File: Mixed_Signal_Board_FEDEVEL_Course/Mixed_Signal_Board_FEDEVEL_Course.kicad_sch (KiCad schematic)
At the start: 0 parts

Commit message: Add Bi filter for Power Sheet
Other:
- added sheet Mixed_Signal_Board_Power (Mixed_Signal_Board_Power.kicad_sch)
- note added: "Hardware Design for Analog Signal Acquisition and Generation Using ADC and DAC"
- note added: "Mixed Signal Board"
- title: (none) -> ${Project_Name}
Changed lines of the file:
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@@
 	(generator_version "10.0")
 	(paper "A4")
+	(title_block
+		(title "${Project_Name}")
+		(date "2026-03-29")
+		(rev "A")
+	)
+	(text "Hardware Design for Analog Signal Acquisition and Generation Using ADC and DAC\n"
+		(exclude_from_sim no)
+		(at 143.51 41.91 0)
+		(effects
+			(font
+				(size 1.27 1.27)
+				(thickness 0.254)
+				(bold yes)
+			)
+		)
+	)
+	(text "Mixed Signal Board"
+		(exclude_from_sim no)
+		(at 144.78 35.56 0)
+		(effects
+			(font
+				(size 4 4)
+				(thickness 0.8)
+				(bold yes)
+				(italic yes)
+				(color 132 0 0 1)
+			)
+		)
+	)
+	(sheet
+		(at 63.5 64.77)
+		(size 41.91 48.26)
+		(exclude_from_sim no)
+		(in_bom yes)
+		(on_board yes)
+		(dnp no)
+		(fields_autoplaced yes)
+		(stroke
+			(width 0.1524)
+			(type solid)
+		)
+		(fill
+			(color 255 255 194 1)
+		)
+		(property "Sheetname" "Mixed_Signal_Board_Power"
+			(at 63.5 64.0584 0)
+			(show_name no)
+			(do_not_autoplace no)
+			(effects
+				(font
+					(size 1.27 1.27)
+				)
+				(justify left bottom)
+			)
+		)
+		(property "Sheetfile" "Mixed_Signal_Board_Power.kicad_sch"
+			(at 63.5 113.6146 0)
+			(show_name no)
+			(do_not_autoplace no)
+			(effects
+				(font
+					(size 1.27 1.27)
+				)
+				(justify left top)
+			)
+		)
+		(instances
+			(project "Mixed_Signal_Board_FEDEVEL_Course"
+				(path "/275c6be1-327e-4739-aa63-a3cb51a55660"
+					(page "2")
+				)
+			)
+		)
+	)
 	(sheet_instances
 		(path "/"

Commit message: Create controller sheet
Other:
- added sheet Mixed_Signal_Board_MCU (Mixed_Signal_Board_MCU.kicad_sch)
- note added: "[1] Power"
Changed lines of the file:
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@@
+		)
+	)
+	(text "[1] Power"
+		(exclude_from_sim no)
+		(at 85.09 88.9 0)
+		(effects
+			(font
+				(size 4 4)
+				(thickness 0.8)
+				(bold yes)
+				(italic yes)
+				(color 0 0 255 1)
+			)
 		)
 	)
@@
 				)
 			)
+		)
+	)
+	(sheet
+		(at 152.4 64.77)
+		(size 43.18 48.26)
+		(exclude_from_sim no)
+		(in_bom yes)
+		(on_board yes)
+		(dnp no)
+		(fields_autoplaced yes)
+		(stroke
+			(width 0.1524)
+			(type solid)
+		)
+		(fill
+			(color 255 255 194 1)
+		)
+		(property "Sheetname" "Mixed_Signal_Board_MCU"
+			(at 152.4 64.0584 0)
+			(show_name no)
+			(do_not_autoplace no)
+			(effects
+				(font
+					(size 1.27 1.27)
+				)
+				(justify left bottom)
+			)
+		)
+		(property "Sheetfile" "Mixed_Signal_Board_MCU.kicad_sch"
+			(at 152.4 113.6146 0)
+			(show_name no)
+			(do_not_autoplace no)
+			(effects
+				(font
+					(size 1.27 1.27)
+				)
+				(justify left top)
+			)
+		)
+		(instances
+			(project "Mixed_Signal_Board_FEDEVEL_Course"
+				(path "/275c6be1-327e-4739-aa63-a3cb51a55660"
+					(page "3")
+				)
+			)

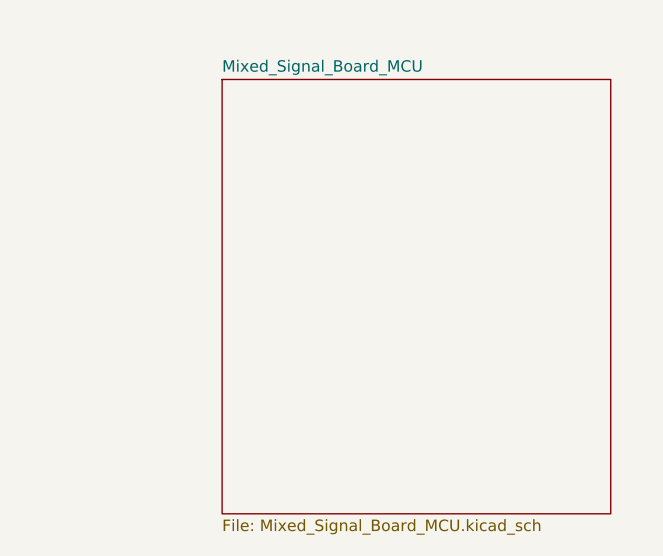
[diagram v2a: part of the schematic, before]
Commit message: Add oscillator circuit for MCU sheet
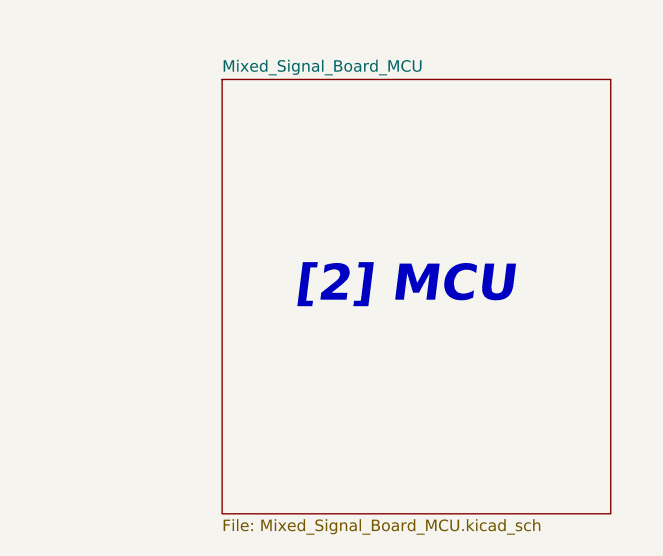
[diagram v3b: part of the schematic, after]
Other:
- note added: "[2] MCU"
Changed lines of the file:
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@@
+		)
+	)
+	(text "[2] MCU\n"
+		(exclude_from_sim no)
+		(at 172.72 87.63 0)
+		(effects
+			(font
+				(size 4 4)
+				(thickness 0.8)
+				(bold yes)
+				(italic yes)
+				(color 0 0 255 1)
+			)
 		)
 	)

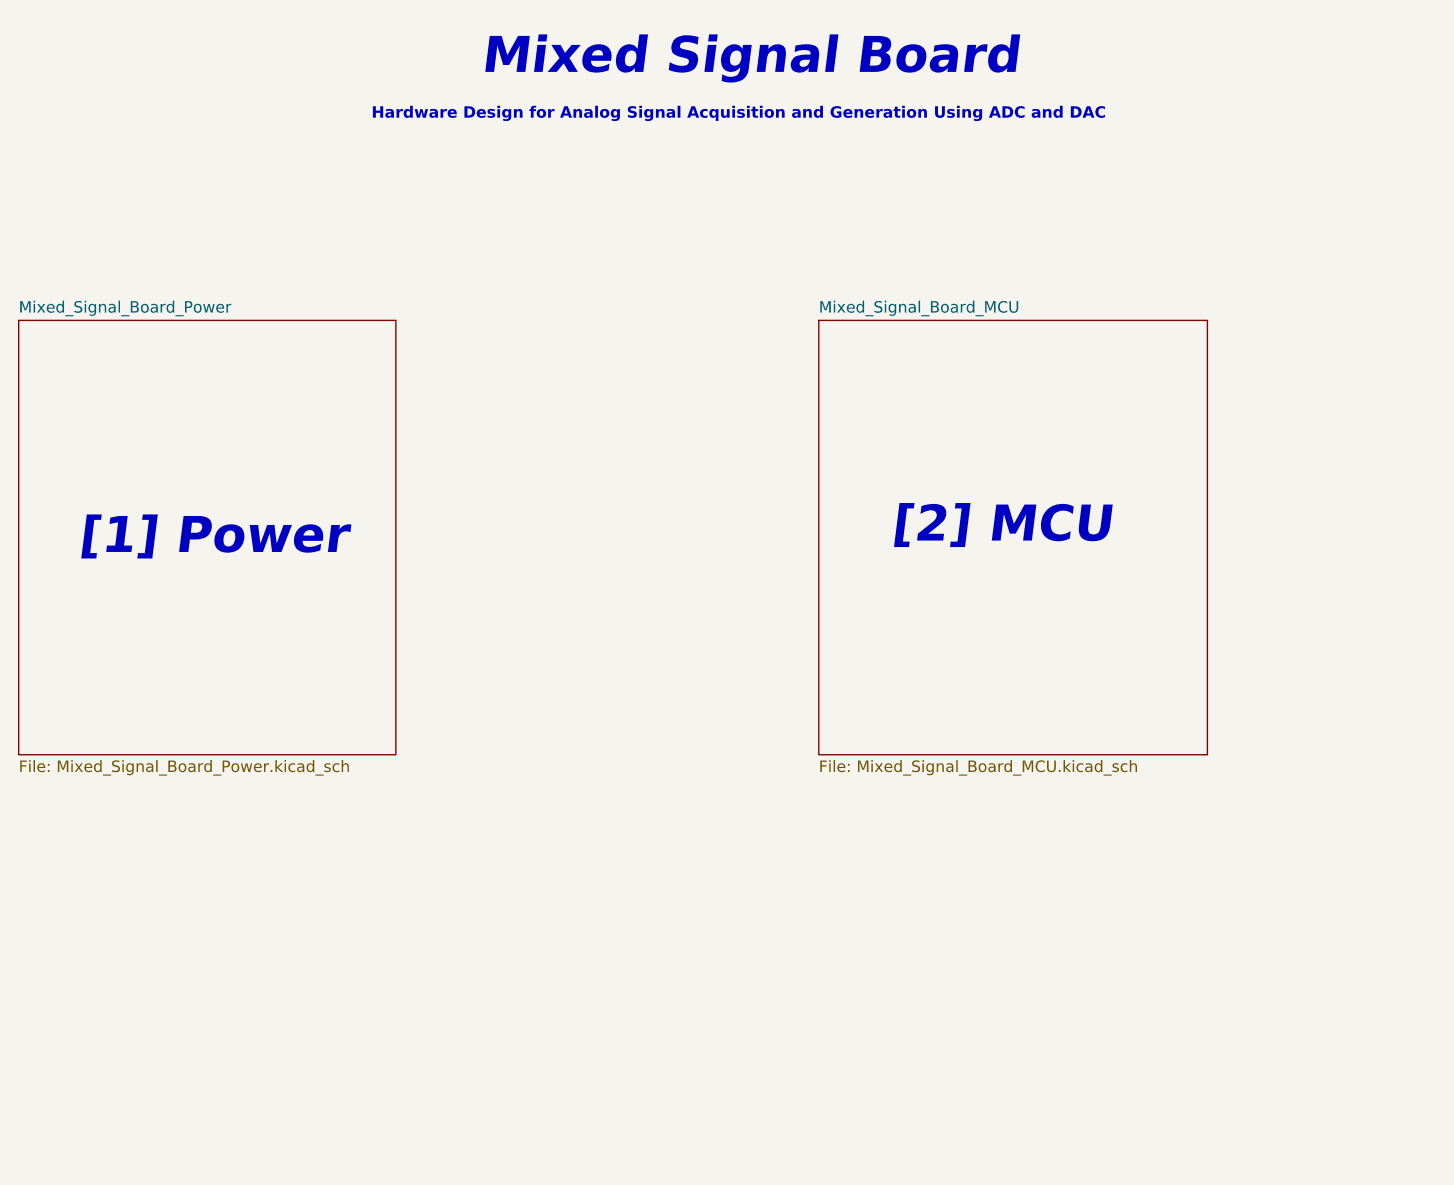
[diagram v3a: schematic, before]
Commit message: Add the sheet of ADC
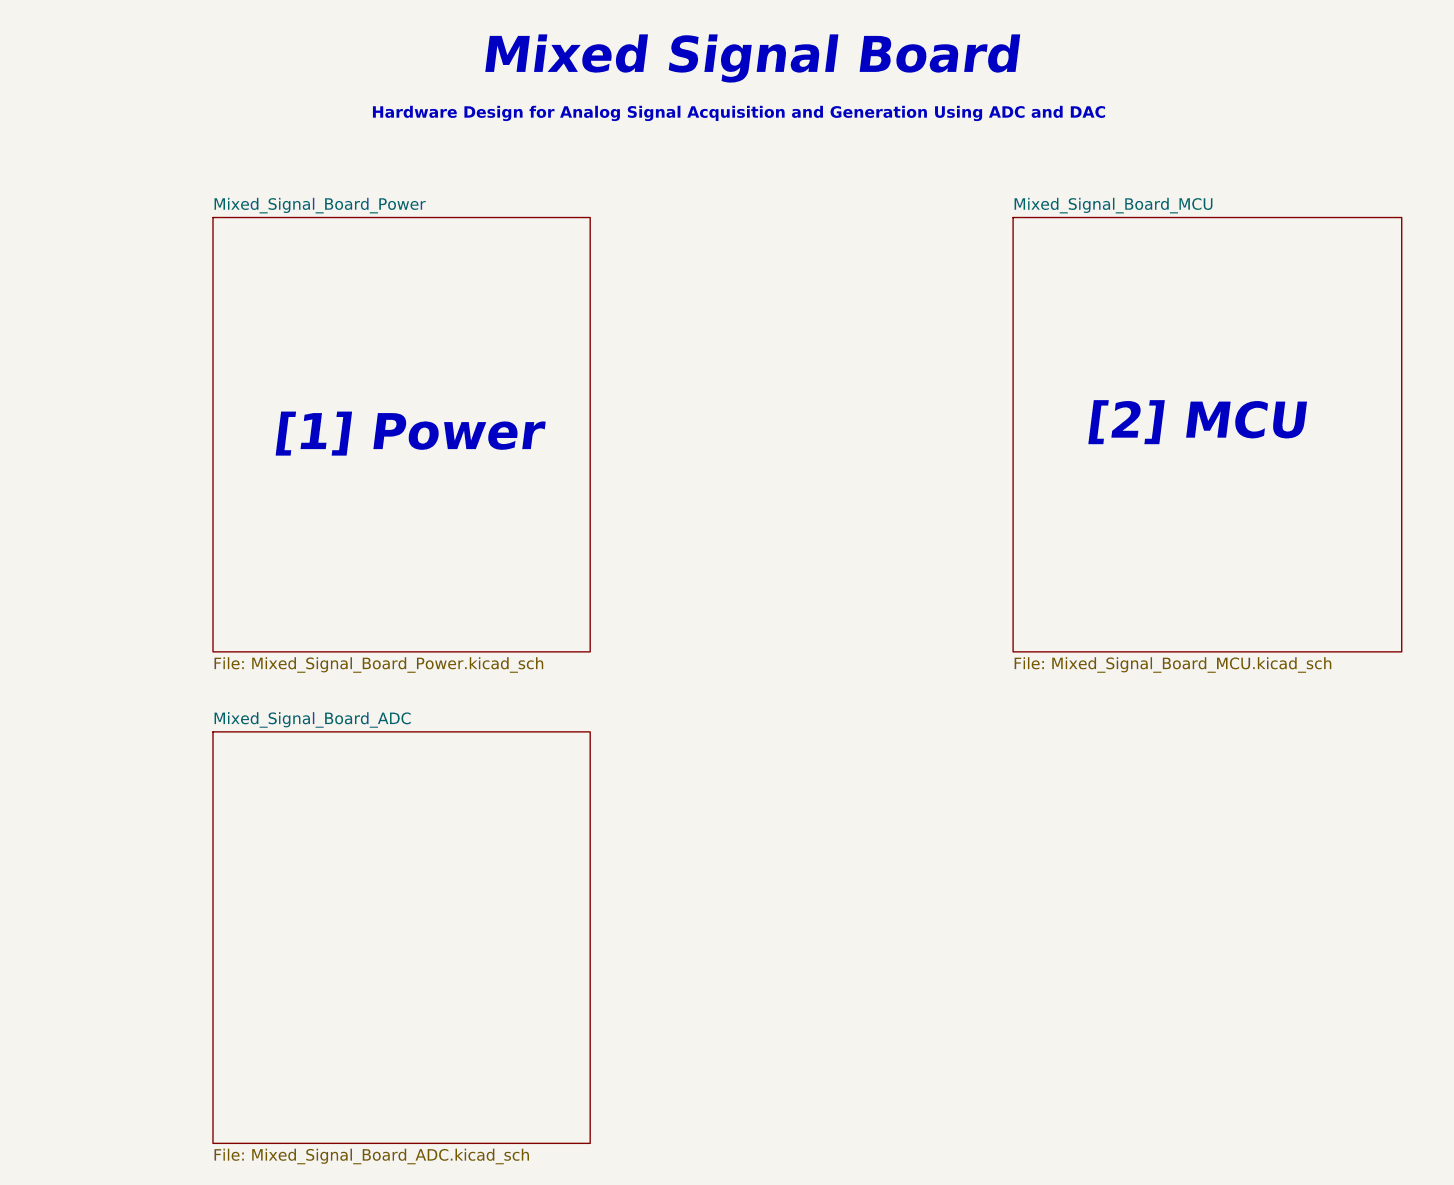
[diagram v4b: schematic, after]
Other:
- added sheet Mixed_Signal_Board_ADC (Mixed_Signal_Board_ADC.kicad_sch)
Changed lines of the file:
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@@
 	(text "[2] MCU\n"
 		(exclude_from_sim no)
-		(at 172.72 87.63 0)
+		(at 194.31 76.2 0)
 		(effects
 			(font
@@
 	(text "[1] Power"
 		(exclude_from_sim no)
-		(at 85.09 88.9 0)
+		(at 106.68 77.47 0)
 		(effects
 			(font
@@
 	)
 	(sheet
-		(at 63.5 64.77)
+		(at 85.09 53.34)
 		(size 41.91 48.26)
 		(exclude_from_sim no)
@@
 		)
 		(property "Sheetname" "Mixed_Signal_Board_Power"
-			(at 63.5 64.0584 0)
+			(at 85.09 52.6284 0)
 			(show_name no)
 			(do_not_autoplace no)
@@
 		)
 		(property "Sheetfile" "Mixed_Signal_Board_Power.kicad_sch"
-			(at 63.5 113.6146 0)
+			(at 85.09 102.1846 0)
 			(show_name no)
 			(do_not_autoplace no)
@@
 	)
 	(sheet
-		(at 152.4 64.77)
+		(at 85.09 110.49)
+		(size 41.91 45.72)
+		(exclude_from_sim no)
+		(in_bom yes)
+		(on_board yes)
+		(dnp no)
+		(fields_autoplaced yes)
+		(stroke
+			(width 0.1524)
+			(type solid)
+		)
+		(fill
+			(color 255 255 194 1)
+		)
+		(property "Sheetname" "Mixed_Signal_Board_ADC"
+			(at 85.09 109.7784 0)
+			(show_name no)
+			(do_not_autoplace no)
+			(effects
+				(font
+					(size 1.27 1.27)
+				)
+				(justify left bottom)
+			)
+		)
+		(property "Sheetfile" "Mixed_Signal_Board_ADC.kicad_sch"
+			(at 85.09 156.7946 0)
+			(show_name no)
+			(do_not_autoplace no)
+			(effects
+				(font
+					(size 1.27 1.27)
+				)
+				(justify left top)
+			)
+		)
+		(instances
+			(project "Mixed_Signal_Board_FEDEVEL_Course"
+				(path "/275c6be1-327e-4739-aa63-a3cb51a55660"
+					(page "4")
+				)
+			)
+		)
+	)
+	(sheet
+		(at 173.99 53.34)
 		(size 43.18 48.26)
 		(exclude_from_sim no)
@@
 		)
 		(property "Sheetname" "Mixed_Signal_Board_MCU"
-			(at 152.4 64.0584 0)
+			(at 173.99 52.6284 0)
 			(show_name no)
 			(do_not_autoplace no)
@@
 		)
 		(property "Sheetfile" "Mixed_Signal_Board_MCU.kicad_sch"
-			(at 152.4 113.6146 0)
+			(at 173.99 102.1846 0)
 			(show_name no)
 			(do_not_autoplace no)

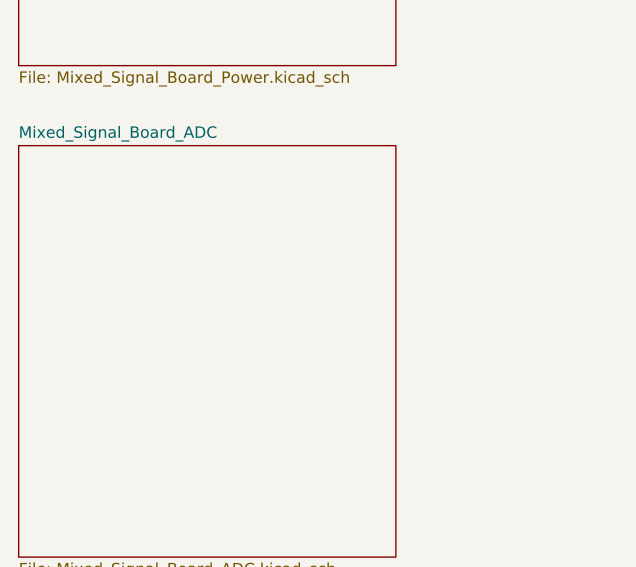
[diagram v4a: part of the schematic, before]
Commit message: Add ADC sch
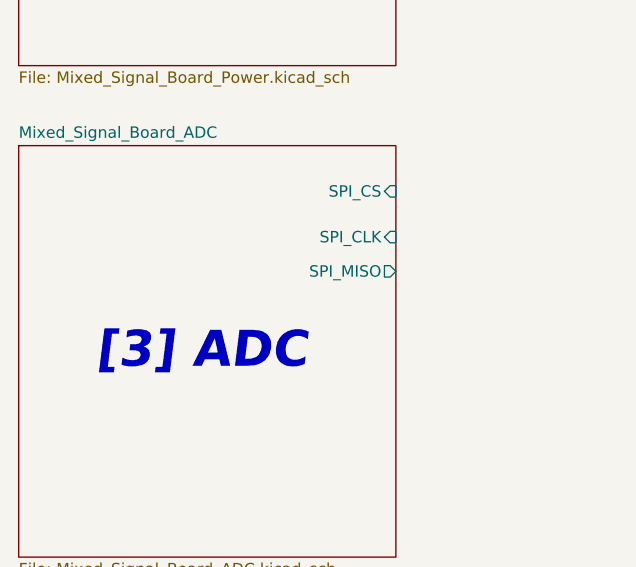
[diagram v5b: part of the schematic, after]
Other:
- sheet Mixed_Signal_Board_ADC ports: added SPI_CLK, SPI_CS, SPI_MISO; removed none
- note added: "[3] ADC"
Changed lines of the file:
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@@
+		)
+	)
+	(text "[3] ADC\n"
+		(exclude_from_sim no)
+		(at 105.41 133.35 0)
+		(effects
+			(font
+				(size 4 4)
+				(thickness 0.8)
+				(bold yes)
+				(italic yes)
+				(color 0 0 255 1)
+			)
 		)
 	)
@@
 			)
 		)
+		(pin "SPI_CS" input
+			(at 127 115.57 0)
+			(effects
+				(font
+					(size 1.27 1.27)
+				)
+				(justify right)
+			)
+		)
+		(pin "SPI_CLK" input
+			(at 127 120.65 0)
+			(effects
+				(font
+					(size 1.27 1.27)
+				)
+				(justify right)
+			)
+		)
+		(pin "SPI_MISO" output
+			(at 127 124.46 0)
+			(effects
+				(font
+					(size 1.27 1.27)
+				)
+				(justify right)
+			)
+		)

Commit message: Compelte the SCH of the project
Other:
- added sheet Mixed_Signal_Board_DAC (Mixed_Signal_Board_DAC.kicad_sch)
- note added: "[3] DAC"
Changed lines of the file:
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@@
+		)
+	)
+	(text "[3] DAC\n"
+		(exclude_from_sim no)
+		(at 195.58 133.35 0)
+		(effects
+			(font
+				(size 4 4)
+				(thickness 0.8)
+				(bold yes)
+				(italic yes)
+				(color 0 0 255 1)
+			)
 		)
 	)
@@
 				)
 			)
+		)
+	)
+	(sheet
+		(at 173.99 110.49)
+		(size 43.18 45.72)
+		(exclude_from_sim no)
+		(in_bom yes)
+		(on_board yes)
+		(dnp no)
+		(fields_autoplaced yes)
+		(stroke
+			(width 0.1524)
+			(type solid)
+		)
+		(fill
+			(color 255 255 194 1)
+		)
+		(property "Sheetname" "Mixed_Signal_Board_DAC"
+			(at 173.99 109.7784 0)
+			(show_name no)
+			(do_not_autoplace no)
+			(effects
+				(font
+					(size 1.27 1.27)
+				)
+				(justify left bottom)
+			)
+		)
+		(property "Sheetfile" "Mixed_Signal_Board_DAC.kicad_sch"
+			(at 173.99 156.7946 0)
+			(show_name no)
+			(do_not_autoplace no)
+			(effects
+				(font
+					(size 1.27 1.27)
+				)
+				(justify left top)
+			)
+		)
+		(instances
+			(project "Mixed_Signal_Board_FEDEVEL_Course"
+				(path "/275c6be1-327e-4739-aa63-a3cb51a55660"
+					(page "5")
+				)
+			)

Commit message: Handle the connections between sheets
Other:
- sheet Mixed_Signal_Board_DAC ports: added DAC_NCLR, DAC_NLDAC, SPI2_MOSI, SPI2_NSS, SPI2_SCK; removed none
- sheet Mixed_Signal_Board_MCU ports: added DAC_NCLR, DAC_NLDAC, SPI2_MOSI, SPI2_NSS, SPI2_SCK, SPI_CLK, SPI_CS, SPI_MISO; removed none
